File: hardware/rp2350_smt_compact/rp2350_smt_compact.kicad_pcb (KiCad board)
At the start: 2 copper layers, 50 x 35 mm, 26 parts, among them J1 RP2350_Zero_SMT_Castellated, J2 USB_A_Neltron_5075AR-04-WH, J3 RP2350_Zero_SMT_Castellated, SW1 SS-12D00G3 SMD SPDT, SW2 SS-12D00G3 SMD SPDT, SW3 SS-12D00G3 SMD SPDT, SW4 SS-12D00G3 SMD SPDT, SW5 SS-12D00G3 SMD SPDT, SW6 PTS645 SMD 6x6 Tact, U1 TPS2051BDBVR, U2 USBLC6-2SC6, U3 USBLC6-2SC6

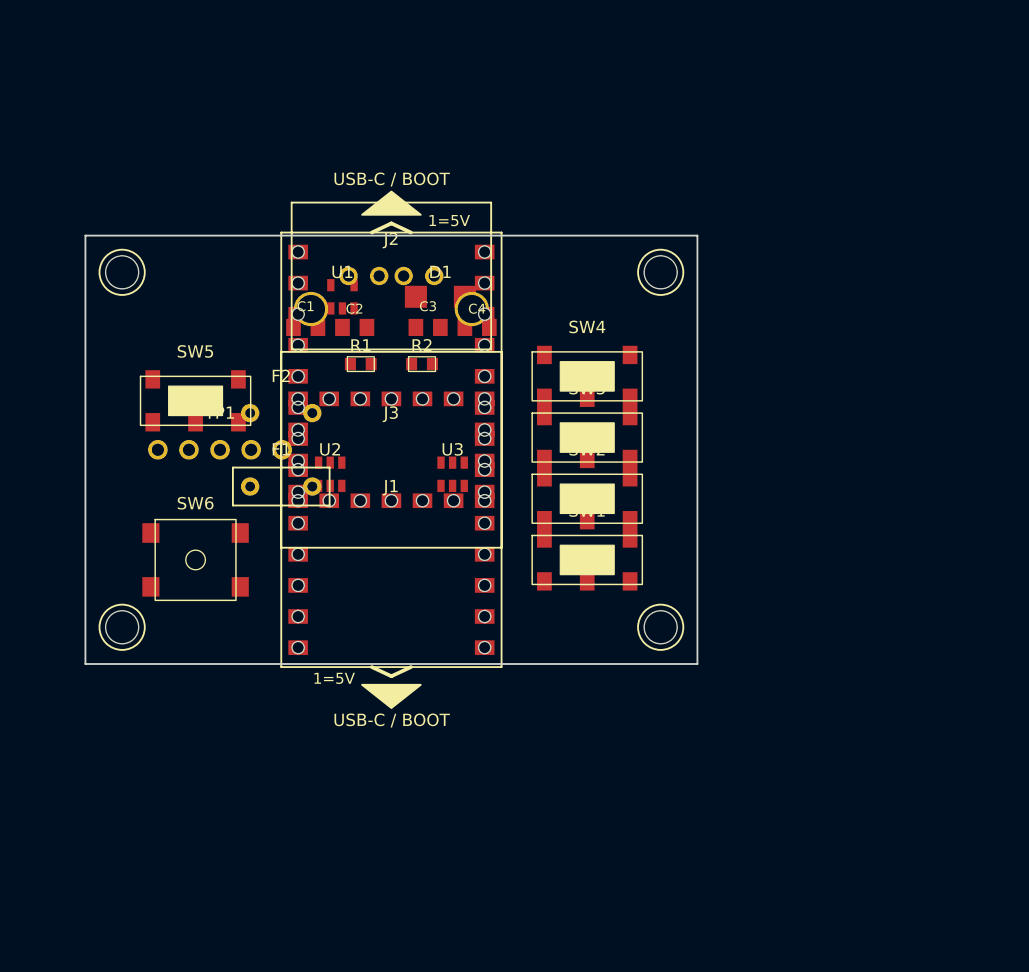
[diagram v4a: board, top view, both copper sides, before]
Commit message: pcb: Edge.Cutsを(0,0)-(50,35)正領域へ移動し紙面クリップ解消
- 従来は中心原点(-25..25/-17.5..17.5)のため kicad-cli pcb export pdf --mode-single で半分が紙面外にクリップされていたため、全footprintとEdge.Cutsを(+25,+17.5)平行移動
- J1(0,6)->(25,23.5)、J3(0,-6)->(25,11.5)、J2(25,3.3)、H1(3,32)/H2(47,32)/H3(3,3)/H4(47,3)ほか相対配置は維持したまま0,0-50,35正領域に収容
- KiCad推奨の正領域配置でPDFがA4内に収まり基板全体が中央に表示、はみ出し0・DRC footprint重なり0を維持
- docs/smt_compact_pcb.pdf/sch.pdf/top.png/3d.pngを再生成してコミット
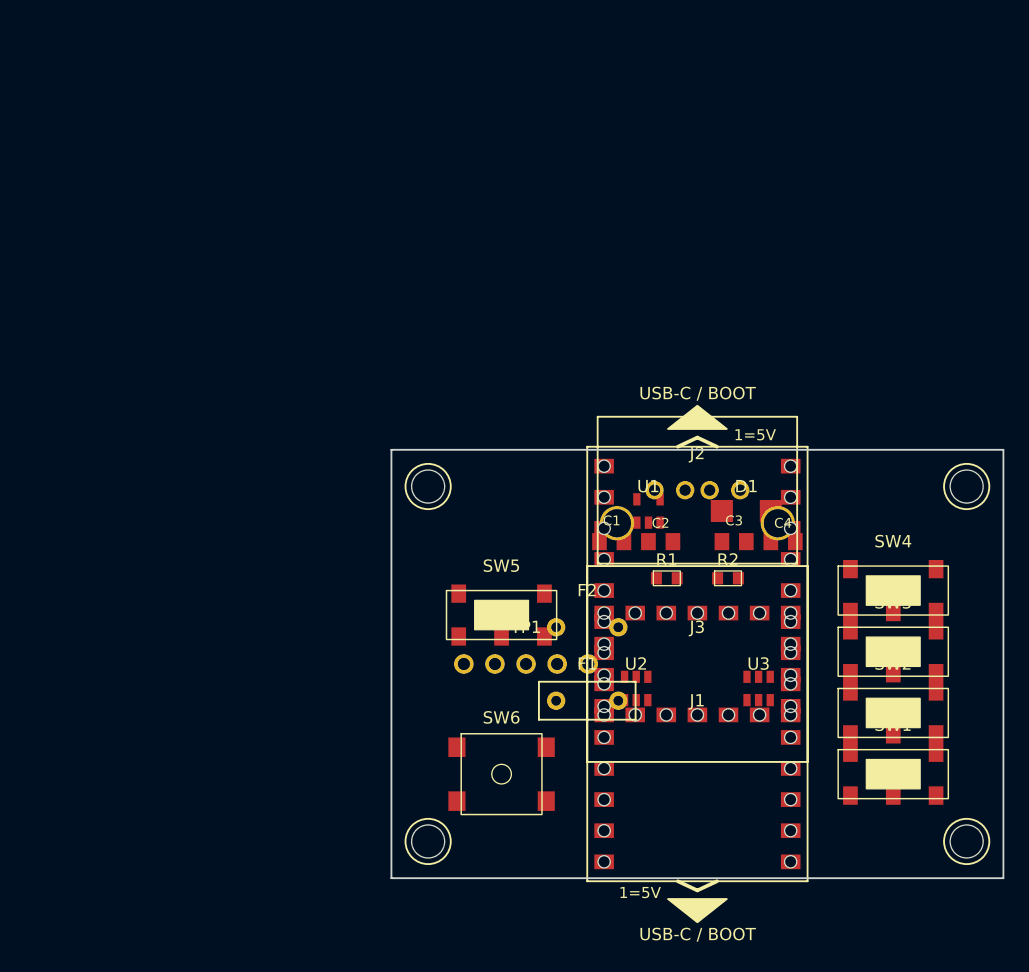
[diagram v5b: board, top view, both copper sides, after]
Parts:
- moved C1 30.5 mm to (18.0, 7.50)
- moved C2 30.5 mm to (22.0, 7.50)
- moved C3 30.5 mm to (28.0, 7.50)
- moved C4 30.5 mm to (32.0, 7.50)
- moved D1 30.5 mm to (29.0, 5.00)
- moved F1 30.5 mm to (16.0, 20.5)
- moved F2 30.5 mm to (16.0, 14.5)
- moved H1 30.5 mm to (3.00, 32.0)
- moved H2 30.5 mm to (47.0, 32.0)
- moved H3 30.5 mm to (3.00, 3.00)
- moved H4 30.5 mm to (47.0, 3.00)
- moved J1 30.5 mm to (25.0, 23.5)
- moved J2 30.5 mm to (25.0, 3.30)
- moved J3 30.5 mm to (25.0, 11.5)
- moved R1 30.5 mm to (22.5, 10.5)
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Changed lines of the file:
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@@
 		(footprint "rp2350_smt_compact:RP2350_Zero_SMT_23p_Castellated"
 		(layer "F.Cu")
-		(at 0 6)
+		(at 25 23.5)
 		(property "Reference" "J1"
 			(at 0 -3 0)
@@
 		(footprint "rp2350_smt_compact:R_0603"
 		(layer "F.Cu")
-		(at -2.5 -7)
+		(at 22.5 10.5)
 		(property "Reference" "R1"
 			(at 0 -1.5 0)
@@
 		(footprint "rp2350_smt_compact:R_0603"
 		(layer "F.Cu")
-		(at 2.5 -7)
+		(at 27.5 10.5)
 		(property "Reference" "R2"
 			(at 0 -1.5 0)
@@
 	(footprint "rp2350_smt_compact:Fuse_Bourns_MF-R050_Radial"
 		(layer "F.Cu")
-		(at -9 3)
+		(at 16 20.5)
 		(property "Reference" "F1"
 			(at 0 -3 0)
@@
 	(footprint "rp2350_smt_compact:USB_A_Neltron_5075AR-04-WH"
 		(layer "F.Cu")
-		(at 0 -14.2)
+		(at 25 3.3)
 		(property "Reference" "J2"
 			(at 0 -3 0)
@@
 		(footprint "rp2350_smt_compact:SW_Slide_SS-12D00_SMD"
 		(layer "F.Cu")
-		(at 16 9)
+		(at 41 26.5)
 		(property "Reference" "SW1"
 			(at 0 -4 0)
@@
 		(footprint "rp2350_smt_compact:SW_Slide_SS-12D00_SMD"
 		(layer "F.Cu")
-		(at 16 4)
+		(at 41 21.5)
 		(property "Reference" "SW2"
 			(at 0 -4 0)
@@
 		(footprint "rp2350_smt_compact:SW_Slide_SS-12D00_SMD"
 		(layer "F.Cu")
-		(at 16 -1)
+		(at 41 16.5)
 		(property "Reference" "SW3"
 			(at 0 -4 0)
@@
 		(footprint "rp2350_smt_compact:SW_Slide_SS-12D00_SMD"
 		(layer "F.Cu")
-		(at 16 -6)
+		(at 41 11.5)
 		(property "Reference" "SW4"
 			(at 0 -4 0)
@@
 		(footprint "rp2350_smt_compact:RP2350_Zero_SMT_23p_Castellated"
 		(layer "F.Cu")
-		(at 0 -6 180)
+		(at 25 11.5 180)
 		(property "Reference" "J3"
 			(at 0 -3 0)
@@
 		(footprint "rp2350_smt_compact:SW_Tact_PTS645_SMD"
 		(layer "F.Cu")
-		(at -16 9)
+		(at 9 26.5)
 		(property "Reference" "SW6"
 			(at 0 -4.6 0)
@@
 		(footprint "rp2350_smt_compact:SW_Slide_SS-12D00_SMD"
 		(layer "F.Cu")
-		(at -16 -4)
+		(at 9 13.5)
 		(property "Reference" "SW5"
 			(at 0 -4 0)
@@
 	(footprint "rp2350_smt_compact:TestPoint_UART0_1x5_P2.54mm"
 		(layer "F.Cu")
-		(at -14 0)
+		(at 11 17.5)
 		(property "Reference" "TP1"
 			(at 0 -3 0)
@@
 	(footprint "rp2350_smt_compact:MountingHole_NPTH_2.7mm"
 		(layer "F.Cu")
-		(at -22 14.5)
+		(at 3 32)
 		(property "Reference" "H1"
 			(at 0 3 0)
@@
 	(footprint "rp2350_smt_compact:MountingHole_NPTH_2.7mm"
 		(layer "F.Cu")
-		(at 22 -14.5)
+		(at 47 3)
 		(property "Reference" "H4"
 			(at 0 4 0)
@@
 	(footprint "rp2350_smt_compact:MountingHole_NPTH_2.7mm"
 		(layer "F.Cu")
-		(at 22 14.5)
+		(at 47 32)
 		(property "Reference" "H2"
 			(at 0 3 0)
@@
 	(footprint "rp2350_smt_compact:MountingHole_NPTH_2.7mm"
 		(layer "F.Cu")
-		(at -22 -14.5)
+		(at 3 3)
 		(property "Reference" "H3"
 			(at 0 4 0)
@@
 	(footprint "rp2350_smt_compact:SOT23-5_TPS2051"
 		(layer "F.Cu")
-		(at -4 -12.5)
+		(at 21 5)
 		(property "Reference" "U1"
 			(at 0 -2 0)
@@
 	(footprint "rp2350_smt_compact:D_SMA_SS14"
 		(layer "F.Cu")
-		(at 4 -12.5)
+		(at 29 5)
 		(property "Reference" "D1"
 			(at 0 -2 0)
@@
 	(footprint "rp2350_smt_compact:C_0805"
 		(layer "F.Cu")
-		(at -7 -10)
+		(at 18 7.5)
 		(property "Reference" "C1"
 			(at 0 -1.7 0)
@@
 	(footprint "rp2350_smt_compact:C_0603"
 		(layer "F.Cu")
-		(at -3 -10)
+		(at 22 7.5)
 		(property "Reference" "C2"
 			(at 0 -1.5 0)
@@
 	(footprint "rp2350_smt_compact:C_0805"
 		(layer "F.Cu")
-		(at 3 -10)
+		(at 28 7.5)
 		(property "Reference" "C3"
 			(at 0 -1.7 0)
@@
 	(footprint "rp2350_smt_compact:C_0603"
 		(layer "F.Cu")
-		(at 7 -10)
+		(at 32 7.5)
 		(property "Reference" "C4"
 			(at 0 -1.5 0)
@@
 	(footprint "rp2350_smt_compact:Fuse_Bourns_MF-R050_Radial"
 		(layer "F.Cu")
-		(at -9 -3)
+		(at 16 14.5)
 		(property "Reference" "F2"
 			(at 0 -3 0)
@@
 	(footprint "rp2350_smt_compact:SOT23-6_USBLC6"
 		(layer "F.Cu")
-		(at -5 2)
+		(at 20 19.5)
 		(property "Reference" "U2"
 			(at 0 -2 0)
@@
 	(footprint "rp2350_smt_compact:SOT23-6_USBLC6"
 		(layer "F.Cu")
-		(at 5 2)
+		(at 30 19.5)
 		(property "Reference" "U3"
 			(at 0 -2 0)
@@
 	)
 	(gr_line
-		(start -25 -17.5)
-		(end 25 -17.5)
+		(start 0 0)
+		(end 50 0)
 		(stroke
 			(width 0.15)
@@
 	)
 	(gr_line
-		(start -25 17.5)
-		(end -25 -17.5)
+		(start 0 35)
+		(end 0 0)
 		(stroke
 			(width 0.15)
@@
 	)
 	(gr_line
-		(start 25 -17.5)
-		(end 25 17.5)
+		(start 50 0)
+		(end 50 35)
 		(stroke
 			(width 0.15)
@@
 	)
 	(gr_line
-		(start 25 17.5)
-		(end -25 17.5)
+		(start 50 35)
+		(end 0 35)
 		(stroke
 			(width 0.15)
